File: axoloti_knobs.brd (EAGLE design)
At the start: 111.7 x 50 mm, 22 parts, among them U1 JOYSTICKPTH

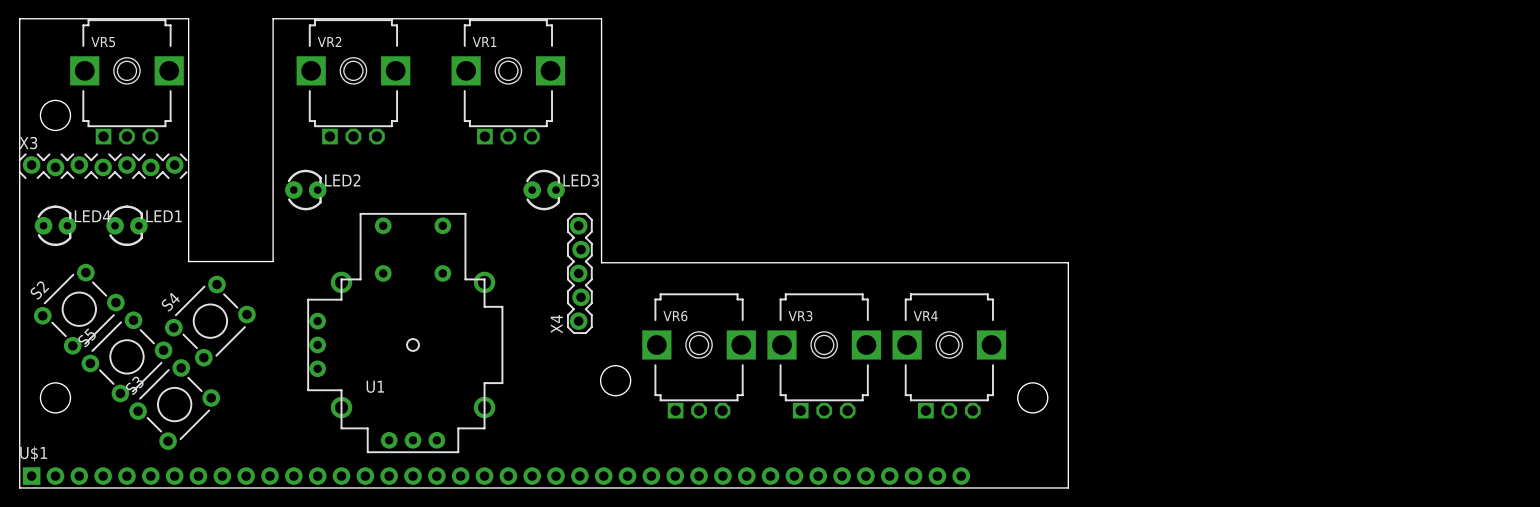
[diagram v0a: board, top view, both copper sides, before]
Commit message: full sized board
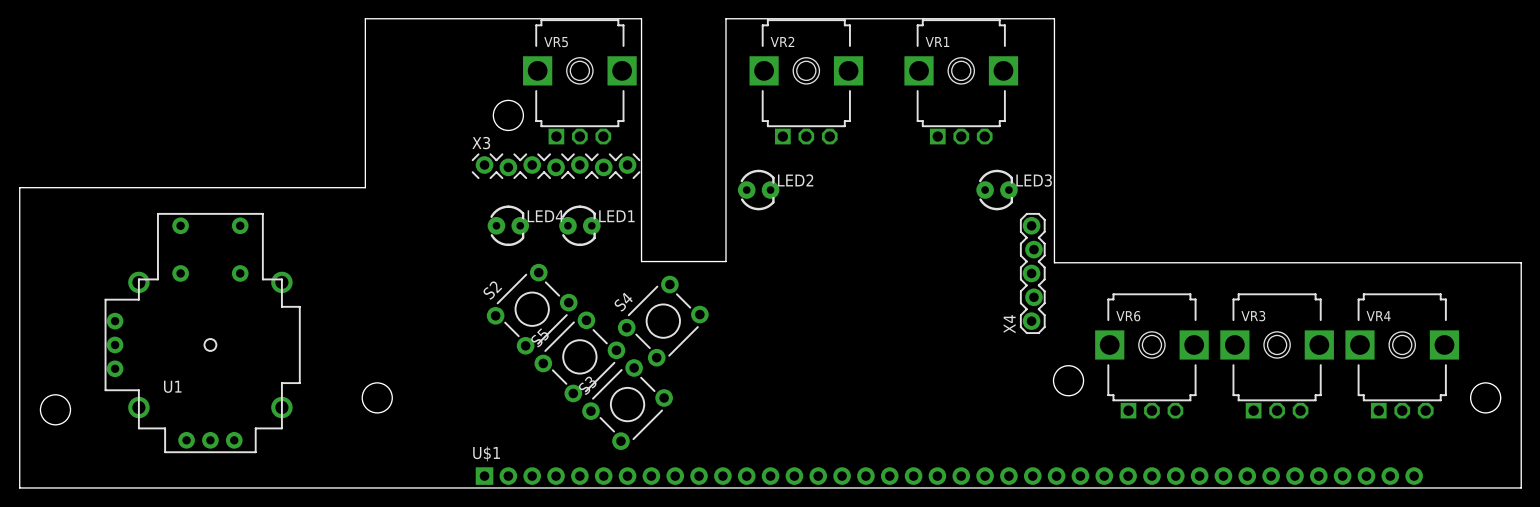
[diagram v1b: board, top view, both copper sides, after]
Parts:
- added U$5: (no value), MusicThingModular:MOUNTING_HOLE
- moved VR3 48.3 mm to (134.0, 15.2)
- moved U$1 48.3 mm to (99.1, 1.27)
- moved U$4 48.3 mm to (156.2, 9.60)
- moved U$6 48.3 mm to (111.8, 11.4)
- moved VR6 48.3 mm to (120.7, 15.2)
- moved X4 48.3 mm to (108.0, 17.8)
- moved LED1 48.3 mm to (59.7, 27.9)
- moved LED3 48.3 mm to (104.1, 31.8)
- moved LED4 48.3 mm to (52.1, 27.9)
- moved S2 48.3 mm to (54.6, 19.1)
- moved S4 48.3 mm to (68.6, 17.8)
- moved S5 48.3 mm to (59.7, 14.0)
- moved U$2 48.3 mm to (52.1, 39.7)
- moved VR1 48.3 mm to (100.3, 44.5)
- moved VR5 48.3 mm to (59.7, 44.5)
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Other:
- board size 111.7 x 50 mm -> 160 x 50 mm
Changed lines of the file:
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@@
 <setting verticaltext="up"/>
 </settings>
-<grid distance="0.05" unitdist="inch" unit="mil" style="lines" multiple="1" display="no" altdistance="0.025" altunitdist="inch" altunit="inch"/>
+<grid distance="0.05" unitdist="inch" unit="mm" style="lines" multiple="1" display="no" altdistance="0.025" altunitdist="inch" altunit="inch"/>
 <layers>
 <layer number="1" name="Top" color="4" fill="1" visible="yes" active="yes"/>
@@
 <board>
 <plain>
-<wire x1="0" y1="0" x2="111.74" y2="0" width="0" layer="20"/>
-<wire x1="111.74" y1="0" x2="111.74" y2="24" width="0" layer="20"/>
-<wire x1="111.74" y1="24" x2="62" y2="24" width="0" layer="20"/>
-<wire x1="62" y1="24" x2="62" y2="50" width="0" layer="20"/>
-<wire x1="62" y1="50" x2="27" y2="50" width="0" layer="20"/>
-<wire x1="27" y1="50" x2="27" y2="24.13" width="0" layer="20"/>
-<wire x1="27" y1="24.13" x2="18" y2="24.13" width="0" layer="20"/>
-<wire x1="18" y1="24.13" x2="18" y2="50" width="0" layer="20"/>
-<wire x1="18" y1="50" x2="0" y2="50" width="0" layer="20"/>
-<wire x1="0" y1="50" x2="0" y2="0" width="0" layer="20"/>
+<wire x1="0" y1="0" x2="160" y2="0" width="0" layer="20"/>
+<wire x1="160" y1="0" x2="160" y2="24" width="0" layer="20"/>
+<wire x1="160" y1="24" x2="110.26" y2="24" width="0" layer="20"/>
+<wire x1="110.26" y1="24" x2="110.26" y2="50" width="0" layer="20"/>
+<wire x1="110.26" y1="50" x2="75.26" y2="50" width="0" layer="20"/>
+<wire x1="75.26" y1="50" x2="75.26" y2="24.13" width="0" layer="20"/>
+<wire x1="75.26" y1="24.13" x2="66.26" y2="24.13" width="0" layer="20"/>
+<wire x1="66.26" y1="24.13" x2="66.26" y2="50" width="0" layer="20"/>
+<wire x1="66.26" y1="50" x2="36.83" y2="50" width="0" layer="20"/>
+<wire x1="36.83" y1="50" x2="36.83" y2="32" width="0" layer="20"/>
+<wire x1="36.83" y1="32" x2="0" y2="32" width="0" layer="20"/>
+<wire x1="0" y1="32" x2="0" y2="0" width="0" layer="20"/>
 </plain>
 <attributes>
@@
 </autorouter>
 <elements>
-<element name="U$1" library="SparkFun-Connectors" package="1X40" value="M40" x="50.8" y="1.27"/>
-<element name="VR1" library="MusicThingModular" package="9MM_SNAP-IN_POT" value="" x="52.07" y="44.45"/>
-<element name="VR2" library="MusicThingModular" package="9MM_SNAP-IN_POT" value="" x="35.56" y="44.45"/>
-<element name="VR3" library="MusicThingModular" package="9MM_SNAP-IN_POT" value="" x="85.725" y="15.24"/>
-<element name="VR4" library="MusicThingModular" package="9MM_SNAP-IN_POT" value="" x="99.06" y="15.24"/>
-<element name="VR5" library="MusicThingModular" package="9MM_SNAP-IN_POT" value="" x="11.43" y="44.45"/>
-<element name="VR6" library="MusicThingModular" package="9MM_SNAP-IN_POT" value="" x="72.39" y="15.24"/>
-<element name="U1" library="SparkFun-Electromechanical" package="JOYSTICK" value="JOYSTICKPTH" x="41.91" y="15.24"/>
-<element name="X4" library="SparkFun-Connectors" package="1X05_LOCK" value="" x="59.69" y="17.78" rot="R90"/>
-<element name="X3" library="SparkFun-Connectors" package="1X07_LOCK" value="" x="1.27" y="34.29"/>
-<element name="U$2" library="MusicThingModular" package="MOUNTING_HOLE" value="" x="3.81" y="39.7"/>
-<element name="U$3" library="MusicThingModular" package="MOUNTING_HOLE" value="" x="3.81" y="9.6"/>
-<element name="U$4" library="MusicThingModular" package="MOUNTING_HOLE" value="" x="107.95" y="9.6"/>
-<element name="U$6" library="MusicThingModular" package="MOUNTING_HOLE" value="" x="63.5" y="11.43"/>
-<element name="S2" library="SparkFun-Electromechanical" package="TACTILE-PTH" value="SWITCH-MOMENTARY-2PTH" x="6.35" y="19.05" rot="R45"/>
-<element name="S3" library="SparkFun-Electromechanical" package="TACTILE-PTH" value="SWITCH-MOMENTARY-2PTH" x="16.51" y="8.89" rot="R45"/>
-<element name="S4" library="SparkFun-Electromechanical" package="TACTILE-PTH" value="SWITCH-MOMENTARY-2PTH" x="20.32" y="17.78" rot="R45"/>
-<element name="S5" library="SparkFun-Electromechanical" package="TACTILE-PTH" value="SWITCH-MOMENTARY-2PTH" x="11.43" y="13.97" rot="R45"/>
-<element name="LED1" library="SparkFun-LED" package="LED3MM" value="" x="11.43" y="27.94"/>
-<element name="LED2" library="SparkFun-LED" package="LED3MM" value="" x="30.48" y="31.75"/>
-<element name="LED3" library="SparkFun-LED" package="LED3MM" value="" x="55.88" y="31.75"/>
-<element name="LED4" library="SparkFun-LED" package="LED3MM" value="" x="3.81" y="27.94"/>
+<element name="U$1" library="SparkFun-Connectors" package="1X40" value="M40" x="99.06" y="1.27"/>
+<element name="VR1" library="MusicThingModular" package="9MM_SNAP-IN_POT" value="" x="100.33" y="44.45"/>
+<element name="VR2" library="MusicThingModular" package="9MM_SNAP-IN_POT" value="" x="83.82" y="44.45"/>
+<element name="VR3" library="MusicThingModular" package="9MM_SNAP-IN_POT" value="" x="133.985" y="15.24"/>
+<element name="VR4" library="MusicThingModular" package="9MM_SNAP-IN_POT" value="" x="147.32" y="15.24"/>
+<element name="VR5" library="MusicThingModular" package="9MM_SNAP-IN_POT" value="" x="59.69" y="44.45"/>
+<element name="VR6" library="MusicThingModular" package="9MM_SNAP-IN_POT" value="" x="120.65" y="15.24"/>
+<element name="U1" library="SparkFun-Electromechanical" package="JOYSTICK" value="JOYSTICKPTH" x="20.32" y="15.24"/>
+<element name="X4" library="SparkFun-Connectors" package="1X05_LOCK" value="" x="107.95" y="17.78" rot="R90"/>
+<element name="X3" library="SparkFun-Connectors" package="1X07_LOCK" value="" x="49.53" y="34.29"/>
+<element name="U$2" library="MusicThingModular" package="MOUNTING_HOLE" value="" x="52.07" y="39.7"/>
+<element name="U$3" library="MusicThingModular" package="MOUNTING_HOLE" value="" x="38.1" y="9.6"/>
+<element name="U$4" library="MusicThingModular" package="MOUNTING_HOLE" value="" x="156.21" y="9.6"/>
+<element name="U$6" library="MusicThingModular" package="MOUNTING_HOLE" value="" x="111.76" y="11.43"/>
+<element name="S2" library="SparkFun-Electromechanical" package="TACTILE-PTH" value="SWITCH-MOMENTARY-2PTH" x="54.61" y="19.05" rot="R45"/>
+<element name="S3" library="SparkFun-Electromechanical" package="TACTILE-PTH" value="SWITCH-MOMENTARY-2PTH" x="64.77" y="8.89" rot="R45"/>
+<element name="S4" library="SparkFun-Electromechanical" package="TACTILE-PTH" value="SWITCH-MOMENTARY-2PTH" x="68.58" y="17.78" rot="R45"/>
+<element name="S5" library="SparkFun-Electromechanical" package="TACTILE-PTH" value="SWITCH-MOMENTARY-2PTH" x="59.69" y="13.97" rot="R45"/>
+<element name="LED1" library="SparkFun-LED" package="LED3MM" value="" x="59.69" y="27.94"/>
+<element name="LED2" library="SparkFun-LED" package="LED3MM" value="" x="78.74" y="31.75"/>
+<element name="LED3" library="SparkFun-LED" package="LED3MM" value="" x="104.14" y="31.75"/>
+<element name="LED4" library="SparkFun-LED" package="LED3MM" value="" x="52.07" y="27.94"/>
+<element name="U$5" library="MusicThingModular" package="MOUNTING_HOLE" value="" x="3.81" y="8.33"/>
 </elements>
 <signals>
@@
 <contactref element="U$1" pad="30"/>
 <contactref element="U$1" pad="29"/>
-<wire x1="72.39" y1="1.27" x2="74.93" y2="1.27" width="0" layer="19" extent="1-1"/>
+<wire x1="120.65" y1="1.27" x2="123.19" y2="1.27" width="0" layer="19" extent="1-1"/>
 </signal>
 <signal name="PB1">
@@
 <contactref element="U$1" pad="21"/>
 <contactref element="U$1" pad="15"/>
-<wire x1="36.83" y1="1.27" x2="52.07" y2="1.27" width="0" layer="19" extent="1-1"/>
+<wire x1="85.09" y1="1.27" x2="100.33" y2="1.27" width="0" layer="19" extent="1-1"/>
 </signal>
 <signal name="PA3">
@@
 <contactref element="U$1" pad="7"/>
 <contactref element="U$1" pad="1"/>
-<wire x1="1.27" y1="1.27" x2="16.51" y2="1.27" width="0" layer="19" extent="1-1"/>
+<wire x1="49.53" y1="1.27" x2="64.77" y2="1.27" width="0" layer="19" extent="1-1"/>
 </signal>
 <signal name="PB9">
@@
 <contactref element="U$1" pad="14"/>
 <contactref element="U$1" pad="6"/>
-<wire x1="82.55" y1="1.27" x2="100.33" y2="1.27" width="0" layer="19" extent="1-1"/>
-<wire x1="80.01" y1="1.27" x2="82.55" y2="1.27" width="0" layer="19" extent="1-1"/>
-<wire x1="69.85" y1="1.27" x2="80.01" y2="1.27" width="0" layer="19" extent="1-1"/>
-<wire x1="49.53" y1="1.27" x2="69.85" y2="1.27" width="0" layer="19" extent="1-1"/>
-<wire x1="34.29" y1="1.27" x2="49.53" y2="1.27" width="0" layer="19" extent="1-1"/>
-<wire x1="13.97" y1="1.27" x2="34.29" y2="1.27" width="0" layer="19" extent="1-1"/>
+<wire x1="130.81" y1="1.27" x2="148.59" y2="1.27" width="0" layer="19" extent="1-1"/>
+<wire x1="128.27" y1="1.27" x2="130.81" y2="1.27" width="0" layer="19" extent="1-1"/>
+<wire x1="118.11" y1="1.27" x2="128.27" y2="1.27" width="0" layer="19" extent="1-1"/>
+<wire x1="97.79" y1="1.27" x2="118.11" y2="1.27" width="0" layer="19" extent="1-1"/>
+<wire x1="82.55" y1="1.27" x2="97.79" y2="1.27" width="0" layer="19" extent="1-1"/>
+<wire x1="62.23" y1="1.27" x2="82.55" y2="1.27" width="0" layer="19" extent="1-1"/>
 </signal>
 <signal name="LOUT+-">

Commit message: full width board
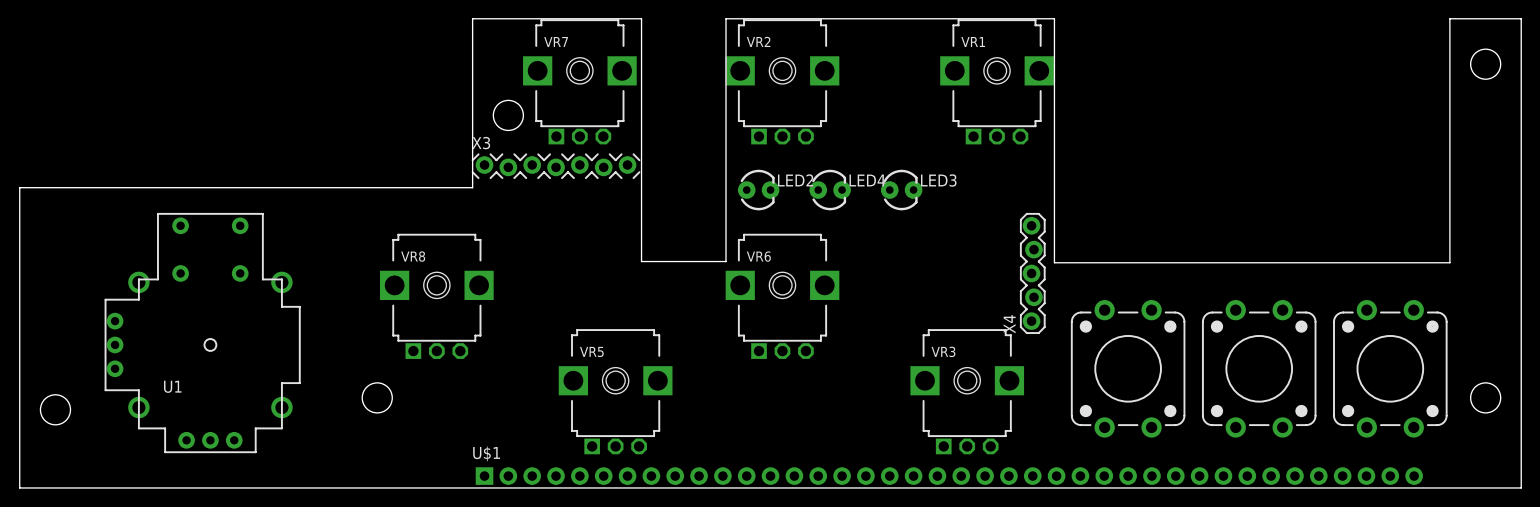
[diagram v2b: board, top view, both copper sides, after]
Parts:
- removed LED1: (no value), SparkFun-LED:LED3MM
- removed S5: SWITCH-MOMENTARY-2PTH, SparkFun-Electromechanical:TACTILE-PTH
- removed U$6: (no value), MusicThingModular:MOUNTING_HOLE
- removed VR4: (no value), MusicThingModular:9MM_SNAP-IN_POT
- added U$7: (no value), MusicThingModular:MOUNTING_HOLE
- added VR7, VR8: (no value), MusicThingModular:9MM_SNAP-IN_POT
- S2, S3, S4: value SWITCH-MOMENTARY-2PTH -> SWITCH-MOMENTARY-212MM; device SparkFun-Electromechanical:TACTILE-PTH -> SparkFun-Electromechanical:TACTILE-PTH-12MM
- moved S4 77.6 mm to (146.1, 12.7), turned to 90 degrees
- moved S3 67.4 mm to (132.1, 12.7), turned to 90 degrees
- moved S2 63.8 mm to (118.1, 12.7), turned to 90 degrees
- moved VR6 39.9 mm to (81.3, 21.6)
- moved LED4 34.5 mm to (86.4, 31.8)
- moved VR3 33.2 mm to (101.0, 11.4)
- moved VR5 33.2 mm to (63.5, 11.4)
- moved LED3 10.2 mm to (94.0, 31.8)
- moved VR1 3.81 mm to (104.1, 44.5)
- moved VR2 2.54 mm to (81.3, 44.5)
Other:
- outline, holes or cut-outs redrawn

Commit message: wip
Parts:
- added U$6: (no value), MusicThingModular:MOUNTING_HOLE
- moved LED3 53.1 mm to (146.1, 21.6)
- moved LED4 46.8 mm to (132.1, 21.6)
- moved LED2 40.7 mm to (118.1, 21.6)
- moved S2 1.27 mm to (118.1, 11.4)
- moved S3 1.27 mm to (132.1, 11.4)
- moved S4 1.27 mm to (146.1, 11.4)
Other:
- outline, holes or cut-outs redrawn
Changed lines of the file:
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@@
 <setting verticaltext="up"/>
 </settings>
-<grid distance="0.05" unitdist="inch" unit="mil" style="lines" multiple="1" display="no" altdistance="0.025" altunitdist="inch" altunit="inch"/>
+<grid distance="0.05" unitdist="inch" unit="mm" style="lines" multiple="1" display="no" altdistance="0.025" altunitdist="inch" altunit="inch"/>
 <layers>
 <layer number="1" name="Top" color="4" fill="1" visible="no" active="yes"/>
@@
 <layer number="15" name="Route15" color="4" fill="6" visible="no" active="no"/>
 <layer number="16" name="Bottom" color="1" fill="1" visible="no" active="yes"/>
-<layer number="17" name="Pads" color="2" fill="1" visible="no" active="yes"/>
+<layer number="17" name="Pads" color="2" fill="1" visible="yes" active="yes"/>
 <layer number="18" name="Vias" color="2" fill="1" visible="no" active="yes"/>
 <layer number="19" name="Unrouted" color="6" fill="1" visible="no" active="yes"/>
@@
 <wire x1="66.26" y1="50" x2="48.26" y2="50" width="0" layer="20"/>
 <wire x1="48.26" y1="50" x2="48.26" y2="32" width="0" layer="20"/>
-<wire x1="48.26" y1="32" x2="0" y2="32" width="0" layer="20"/>
-<wire x1="0" y1="32" x2="0" y2="0" width="0" layer="20"/>
+<wire x1="48.26" y1="32" x2="7.62" y2="32" width="0" layer="20"/>
+<wire x1="7.62" y1="32" x2="7.62" y2="50" width="0" layer="20"/>
+<wire x1="7.62" y1="50" x2="0" y2="50" width="0" layer="20"/>
+<wire x1="0" y1="50" x2="0" y2="0" width="0" layer="20"/>
 </plain>
 <attributes>
@@
 <element name="U$3" library="MusicThingModular" package="MOUNTING_HOLE" value="" x="38.1" y="9.6"/>
 <element name="U$4" library="MusicThingModular" package="MOUNTING_HOLE" value="" x="156.21" y="9.6"/>
-<element name="S2" library="SparkFun-Electromechanical" package="TACTILE-PTH-12MM" value="SWITCH-MOMENTARY-212MM" x="118.11" y="12.7" rot="R90">
-<attribute name="PROD_ID" value="SWCH-09185" x="118.11" y="12.7" size="1.778" layer="27" rot="R90" display="off"/>
+<element name="S2" library="SparkFun-Electromechanical" package="TACTILE-PTH-12MM" value="SWITCH-MOMENTARY-212MM" x="118.11" y="11.43" rot="R90">
+<attribute name="PROD_ID" value="SWCH-09185" x="118.11" y="11.43" size="1.778" layer="27" rot="R90" display="off"/>
 </element>
-<element name="S3" library="SparkFun-Electromechanical" package="TACTILE-PTH-12MM" value="SWITCH-MOMENTARY-212MM" x="132.08" y="12.7" rot="R90">
-<attribute name="PROD_ID" value="SWCH-09185" x="132.08" y="12.7" size="1.778" layer="27" rot="R90" display="off"/>
+<element name="S3" library="SparkFun-Electromechanical" package="TACTILE-PTH-12MM" value="SWITCH-MOMENTARY-212MM" x="132.08" y="11.43" rot="R90">
+<attribute name="PROD_ID" value="SWCH-09185" x="132.08" y="11.43" size="1.778" layer="27" rot="R90" display="off"/>
 </element>
-<element name="S4" library="SparkFun-Electromechanical" package="TACTILE-PTH-12MM" value="SWITCH-MOMENTARY-212MM" x="146.05" y="12.7" rot="R90">
-<attribute name="PROD_ID" value="SWCH-09185" x="146.05" y="12.7" size="1.778" layer="27" rot="R90" display="off"/>
+<element name="S4" library="SparkFun-Electromechanical" package="TACTILE-PTH-12MM" value="SWITCH-MOMENTARY-212MM" x="146.05" y="11.43" rot="R90">
+<attribute name="PROD_ID" value="SWCH-09185" x="146.05" y="11.43" size="1.778" layer="27" rot="R90" display="off"/>
 </element>
-<element name="LED2" library="SparkFun-LED" package="LED3MM" value="" x="78.74" y="31.75"/>
-<element name="LED3" library="SparkFun-LED" package="LED3MM" value="" x="93.98" y="31.75"/>
-<element name="LED4" library="SparkFun-LED" package="LED3MM" value="" x="86.36" y="31.75"/>
+<element name="LED2" library="SparkFun-LED" package="LED3MM" value="" x="118.11" y="21.59"/>
+<element name="LED3" library="SparkFun-LED" package="LED3MM" value="" x="146.05" y="21.59"/>
+<element name="LED4" library="SparkFun-LED" package="LED3MM" value="" x="132.08" y="21.59"/>
 <element name="U$5" library="MusicThingModular" package="MOUNTING_HOLE" value="" x="3.81" y="8.33"/>
 <element name="VR7" library="MusicThingModular" package="9MM_SNAP-IN_POT" value="" x="59.69" y="44.45"/>
 <element name="VR8" library="MusicThingModular" package="9MM_SNAP-IN_POT" value="" x="44.45" y="21.59"/>
 <element name="U$7" library="MusicThingModular" package="MOUNTING_HOLE" value="" x="156.21" y="45.16"/>
+<element name="U$6" library="MusicThingModular" package="MOUNTING_HOLE" value="" x="3.81" y="45.16"/>
 </elements>
 <signals>
